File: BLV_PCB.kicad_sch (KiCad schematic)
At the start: 10 parts, among them J1 Cube0_UART_JST-PH, J2 Cube0_UART_JST-PH, J3 Cube0_UART_JST-PH, J4 Cube0_UART_Debug, J5 Cube0_UART_Debug, J6 Cube0_UART_Debug

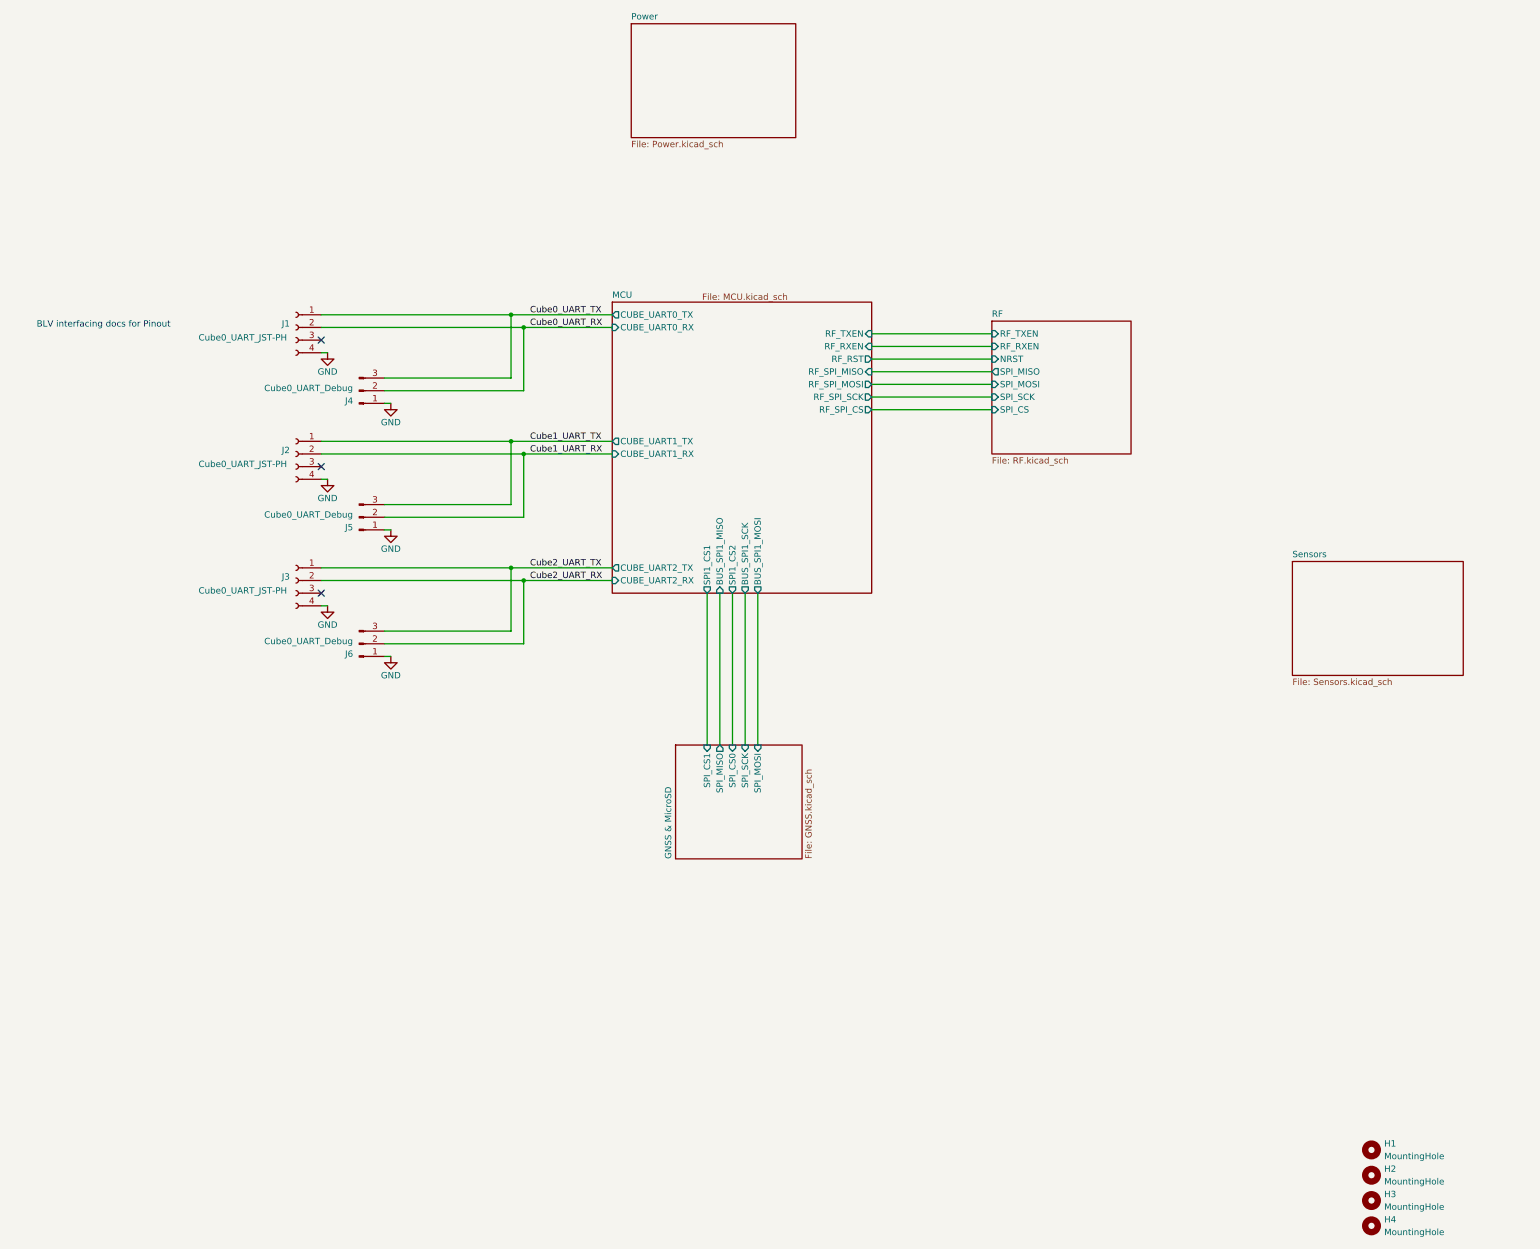
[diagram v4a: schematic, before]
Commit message: General DFM fixes
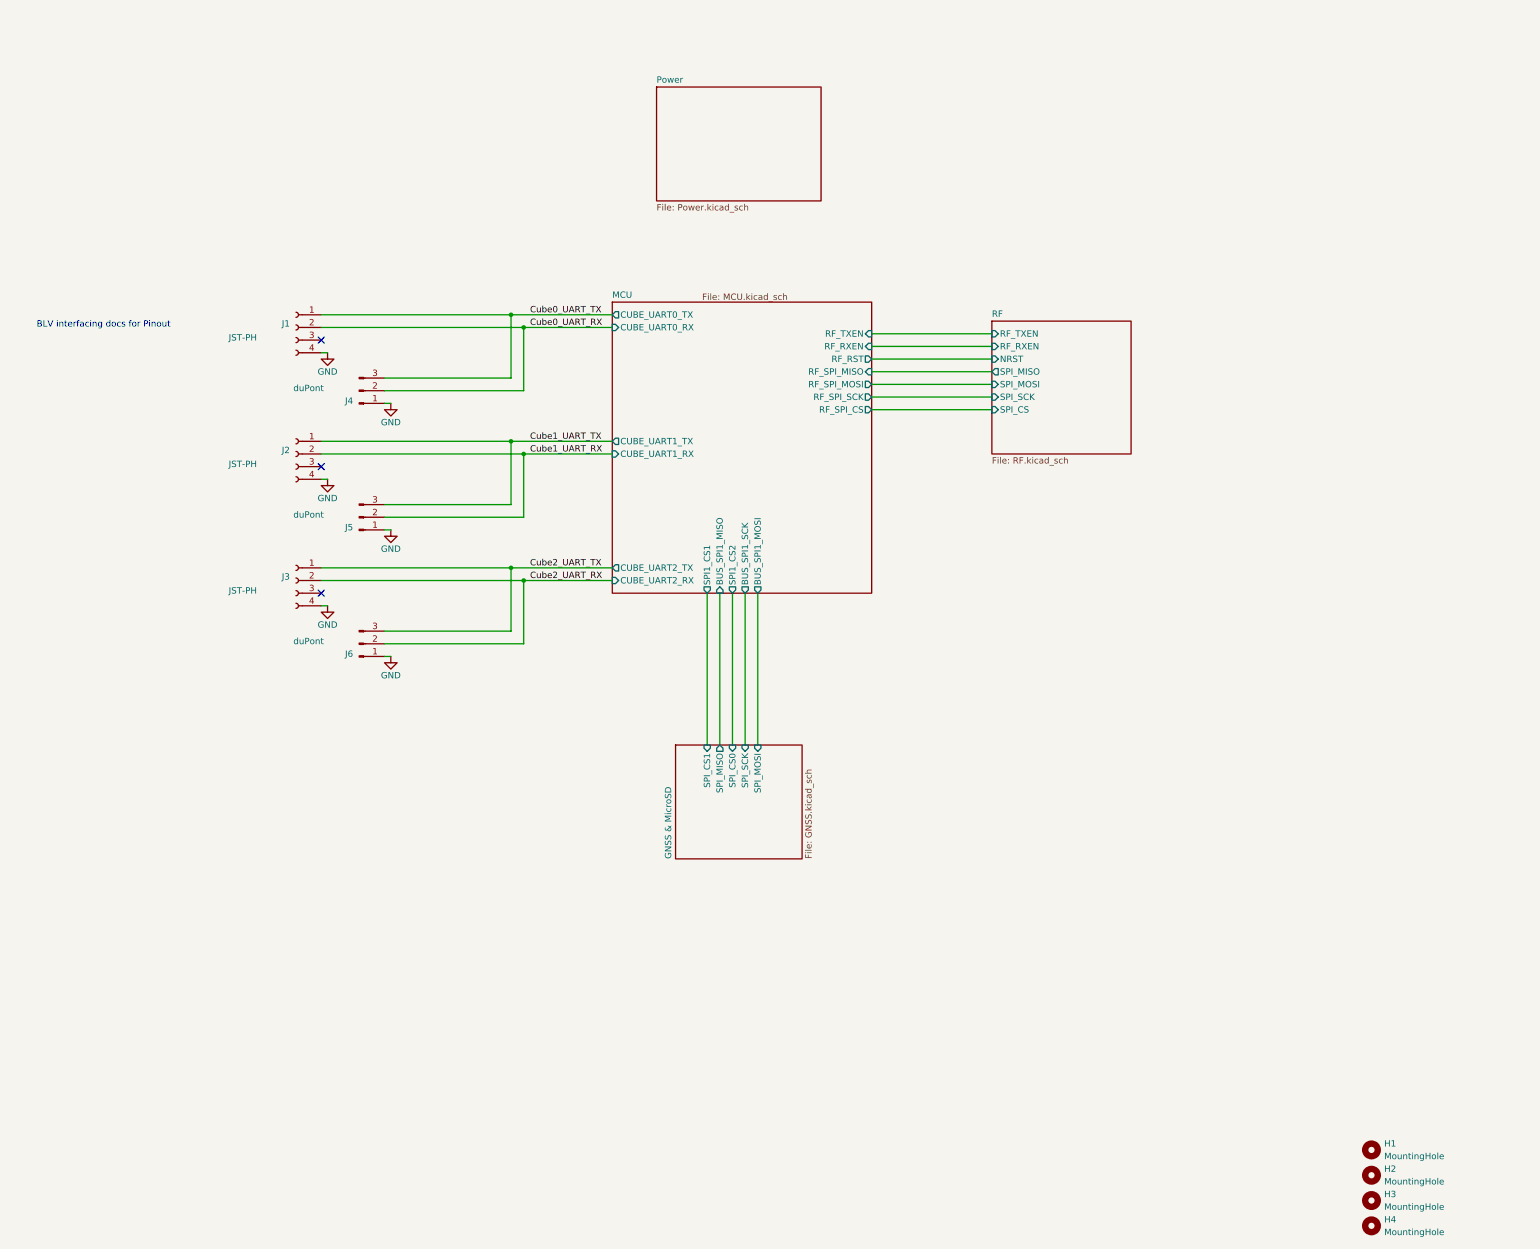
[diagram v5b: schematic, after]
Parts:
- H1, H2, H3, H4: footprint MountingHole:MountingHole_3.2mm_M3 -> MountingHole:MountingHole_3.2mm_M3_DIN965_Pad
- J1, J2, J3: value Cube0_UART_JST-PH -> JST-PH; footprint Connector_JST:JST_PH_S4B-PH-K_1x04_P2.00mm_Horizontal -> Connector_JST:JST_PH_B4B-PH-K_1x04_P2.00mm_Vertical; LCSC Part (none) -> C131334
- J4, J5, J6: value Cube0_UART_Debug -> duPont
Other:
- removed sheet Sensors
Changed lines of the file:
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@@
 			)
 		)
-		(property "Value" "Cube0_UART_JST-PH"
+		(property "Value" "JST-PH"
 			(at 65.532 108.712 0)
 			(effects
@@
 			)
 		)
-		(property "Footprint" "Connector_JST:JST_PH_S4B-PH-K_1x04_P2.00mm_Horizontal"
+		(property "Footprint" "Connector_JST:JST_PH_B4B-PH-K_1x04_P2.00mm_Vertical"
 			(at 76.2 106.68 0)
 			(effects
@@
 		)
 		(property "SnapEDA_Link" ""
+			(at 76.2 106.68 0)
+			(effects
+				(font
+					(size 1.27 1.27)
+				)
+				(hide yes)
+			)
+		)
+		(property "LCSC Part" "C131334"
 			(at 76.2 106.68 0)
 			(effects
@@
 			)
 		)
-		(property "Value" "Cube0_UART_Debug"
+		(property "Value" "duPont"
 			(at 78.74 144.272 0)
 			(effects
@@
 			)
 		)
-		(property "Value" "Cube0_UART_JST-PH"
+		(property "Value" "JST-PH"
 			(at 65.532 134.112 0)
 			(effects
@@
 			)
 		)
-		(property "Footprint" "Connector_JST:JST_PH_S4B-PH-K_1x04_P2.00mm_Horizontal"
+		(property "Footprint" "Connector_JST:JST_PH_B4B-PH-K_1x04_P2.00mm_Vertical"
 			(at 76.2 132.08 0)
 			(effects
@@
 		)
 		(property "SnapEDA_Link" ""
+			(at 76.2 132.08 0)
+			(effects
+				(font
+					(size 1.27 1.27)
+				)
+				(hide yes)
+			)
+		)
+		(property "LCSC Part" "C131334"
 			(at 76.2 132.08 0)
 			(effects
@@
 			)
 		)
-		(property "Footprint" "MountingHole:MountingHole_3.2mm_M3"
+		(property "Footprint" "MountingHole:MountingHole_3.2mm_M3_DIN965_Pad"
 			(at 292.1 251.46 0)
 			(effects
@@
 			)
 		)
-		(property "Value" "Cube0_UART_JST-PH"
+		(property "Value" "JST-PH"
 			(at 65.532 83.312 0)
 			(effects
@@
 			)
 		)
-		(property "Footprint" "Connector_JST:JST_PH_S4B-PH-K_1x04_P2.00mm_Horizontal"
+		(property "Footprint" "Connector_JST:JST_PH_B4B-PH-K_1x04_P2.00mm_Vertical"
 			(at 76.2 81.28 0)
 			(effects
@@
 		)
 		(property "SnapEDA_Link" ""
+			(at 76.2 81.28 0)
+			(effects
+				(font
+					(size 1.27 1.27)
+				)
+				(hide yes)
+			)
+		)
+		(property "LCSC Part" "C131334"
 			(at 76.2 81.28 0)
 			(effects
@@
 			)
 		)
-		(property "Footprint" "MountingHole:MountingHole_3.2mm_M3"
+		(property "Footprint" "MountingHole:MountingHole_3.2mm_M3_DIN965_Pad"
 			(at 292.1 256.54 0)
 			(effects
@@
 			)
 		)
-		(property "Footprint" "MountingHole:MountingHole_3.2mm_M3"
+		(property "Footprint" "MountingHole:MountingHole_3.2mm_M3_DIN965_Pad"
 			(at 292.1 261.62 0)
 			(effects
@@
 			)
 		)
-		(property "Value" "Cube0_UART_Debug"
+		(property "Value" "duPont"
 			(at 78.74 93.472 0)
 			(effects
@@
 			)
 		)
-		(property "Footprint" "MountingHole:MountingHole_3.2mm_M3"
+		(property "Footprint" "MountingHole:MountingHole_3.2mm_M3_DIN965_Pad"
 			(at 292.1 246.38 0)
 			(effects
@@
 			)
 		)
-		(property "Value" "Cube0_UART_Debug"
+		(property "Value" "duPont"
 			(at 78.74 118.872 0)
 			(effects
@@
 	)
 	(sheet
-		(at 143.51 20.32)
+		(at 148.59 33.02)
 		(size 33.02 22.86)
 		(exclude_from_sim no)
@@
 		)
 		(property "Sheetname" "Power"
-			(at 143.51 19.6084 0)
+			(at 148.59 32.3084 0)
 			(effects
 				(font
@@
 		)
 		(property "Sheetfile" "Power.kicad_sch"
-			(at 143.51 43.7646 0)
+			(at 148.59 56.4646 0)
 			(effects
 				(font
@@
 		)
 		(property "Field2" ""
-			(at 143.51 20.32 0)
+			(at 148.59 33.02 0)
 			(effects
 				(font
@@
 				)
 			)
-		)
-	)
-	(sheet
-		(at 276.225 128.27)
-		(size 34.29 22.86)
-		(exclude_from_sim no)
-		(in_bom yes)
-		(on_board yes)
-		(dnp no)
-		(fields_autoplaced yes)
-		(stroke
-			(width 0.1524)
-			(type solid)
-		)
-		(fill
-			(color 0 0 0 0.0000)
-		)
-		(property "Sheetname" "Sensors"
-			(at 276.225 127.5584 0)
-			(effects
-				(font
-					(size 1.27 1.27)
-				)
-				(justify left bottom)
-			)
-		)
-		(property "Sheetfile" "Sensors.kicad_sch"
-			(at 276.225 151.7146 0)
-			(effects
-				(font
-					(size 1.27 1.27)
-				)
-				(justify left top)
-			)
-		)
-		(instances
-			(project "BLV_PCB"
-				(path "/e98ed281-6a46-49b2-ab41-e3d95fdf6973"
-					(page "4")
-				)
-			)
